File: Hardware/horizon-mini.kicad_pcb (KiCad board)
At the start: 2 copper layers, 35 x 35.5 mm, 81 parts, among them J2 Conn_01x02_Pin, J3 Micro_SD_Card_Det1, J7 USB_C_Receptacle_USB2.0_16P, J8 Conn_02x03_Counter_Clockwise, Q1 BSS138, Q10 DMG2301L, U1 TPS82130, U16 AP2112K-3.3, U2 TPS61092, U3 LTC4412xS6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

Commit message: Finally done... DRC look good, PCB is good, and schematic looks good!
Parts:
- added R5: 10kΩ, Resistor_SMD:R_0402_1005Metric, B.Cu at (151.1, 118.9)
- C78: footprint Capacitor_SMD:C_0603_1608Metric -> Capacitor_SMD:C_0402_1005Metric
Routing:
- net MISO TMCU: track 50.7 -> 47.8 mm, vias 7 -> 4
- net +3.3V: track 155.7 -> 158.2 mm, vias 9 -> 10
- net GND: track 120.0 -> 121.6 mm, vias 31 -> 134
- net CS_NAND MMCU: track 32.2 -> 33.6 mm
- net CS_SD MMCU: track 34.0 -> 35.2 mm
- net MOSI TMCU: track 32.4 -> 33.2 mm, vias 4 -> 3
- net BUZZER: track 41.3 -> 42.0 mm
- net Net-(U7-~{CS}): track 2.13 -> 1.47 mm
- net +5V: track 9.82 -> 9.23 mm
- net (no net): vias 0 -> 2
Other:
- board size 35 x 35.5 mm -> 36 x 36 mm

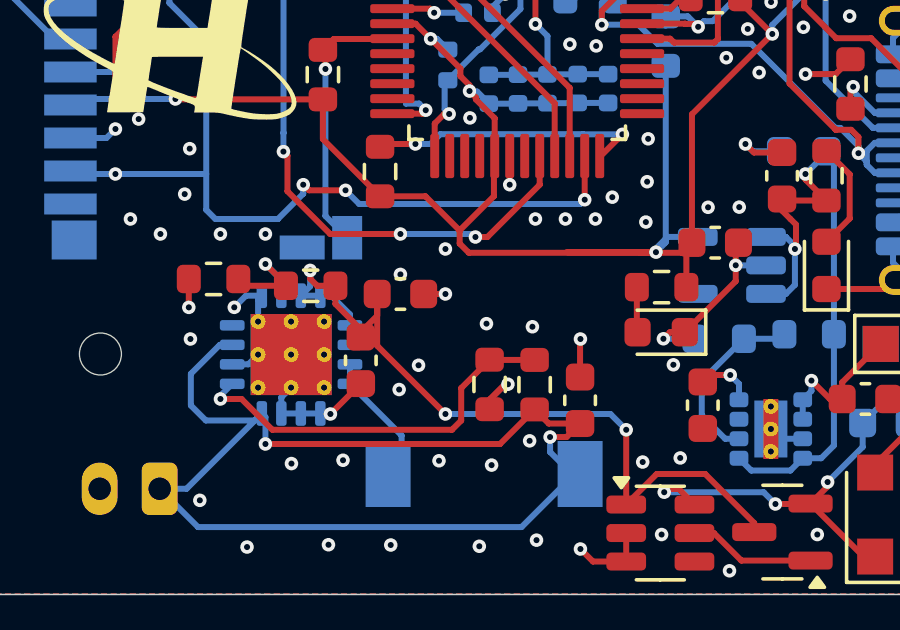
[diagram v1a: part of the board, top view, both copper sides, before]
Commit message: now final ;)... Needed to switch the 100uF to 0206, since 0603's for that just don't exist!
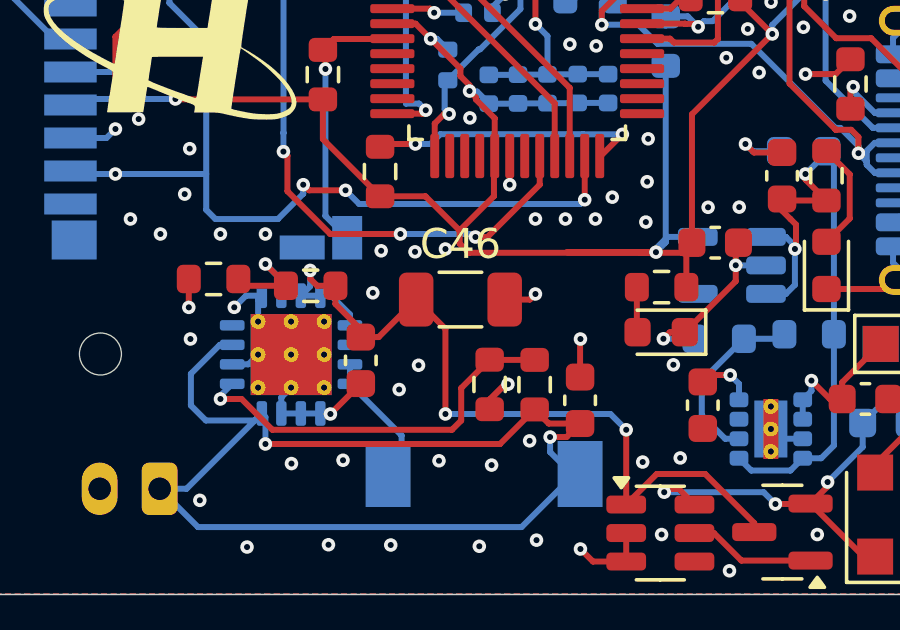
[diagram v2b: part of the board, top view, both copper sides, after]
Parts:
- C46: value 100u -> 100uF; footprint Capacitor_SMD:C_0603_1608Metric -> Capacitor_SMD:C_1206_3216Metric
- moved C46 2.01 mm to (151.5, 126.7)
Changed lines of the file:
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@@
 		)
 	)
-	(footprint "Capacitor_SMD:C_0603_1608Metric"
+	(footprint "Capacitor_SMD:C_1206_3216Metric"
 		(layer "F.Cu")
-		(at 149.5 126.5)
-		(descr "Capacitor SMD 0603 (1608 Metric), square (rectangular) end terminal, IPC-7351 nominal, (Body size source: IPC-SM-782 page 76, https://www.pcb-3d.com/wordpress/wp-content/uploads/ipc-sm-782a_amendment_1_and_2.pdf), generated with kicad-footprint-generator")
+		(at 151.5 126.685172)
+		(descr "Capacitor SMD 1206 (3216 Metric), square (rectangular) end terminal, IPC-7351 nominal, (Body size source: IPC-SM-782 page 76, https://www.pcb-3d.com/wordpress/wp-content/uploads/ipc-sm-782a_amendment_1_and_2.pdf), generated with kicad-footprint-generator")
 		(tags "capacitor")
 		(property "Reference" "C46"
-			(at 0 -1.43 0)
+			(at 0 -1.85 0)
 			(layer "F.SilkS")
-			(hide yes)
 			(effects
 				(font
@@
 			)
 		)
-		(property "Value" "100u"
-			(at 0 1.43 0)
+		(property "Value" "100uF"
+			(at 0 1.85 0)
 			(layer "F.Fab")
 			(effects
@@
 			)
 		)
-		(property "Description" "Polarized capacitor, US symbol"
+		(property "Description" ""
 			(at 0 0 0)
 			(layer "F.Fab")
@@
 		(attr smd)
 		(fp_line
-			(start -0.14058 -0.51)
-			(end 0.14058 -0.51)
+			(start -0.711252 -0.91)
+			(end 0.711252 -0.91)
 			(stroke
 				(width 0.12)
@@
 		)
 		(fp_line
-			(start -0.14058 0.51)
-			(end 0.14058 0.51)
+			(start -0.711252 0.91)
+			(end 0.711252 0.91)
 			(stroke
 				(width 0.12)
@@
 		)
 		(fp_line
-			(start -1.48 -0.73)
-			(end 1.48 -0.73)
+			(start -2.3 -1.15)
+			(end 2.3 -1.15)
 			(stroke
 				(width 0.05)
@@
 		)
 		(fp_line
-			(start -1.48 0.73)
-			(end -1.48 -0.73)
+			(start -2.3 1.15)
+			(end -2.3 -1.15)
 			(stroke
 				(width 0.05)
@@
 		)
 		(fp_line
-			(start 1.48 -0.73)
-			(end 1.48 0.73)
+			(start 2.3 -1.15)
+			(end 2.3 1.15)
 			(stroke
 				(width 0.05)
@@
 		)
 		(fp_line
-			(start 1.48 0.73)
-			(end -1.48 0.73)
+			(start 2.3 1.15)
+			(end -2.3 1.15)
 			(stroke
 				(width 0.05)
@@
 		)
 		(fp_line
-			(start -0.8 -0.4)
-			(end 0.8 -0.4)
+			(start -1.6 -0.8)
+			(end 1.6 -0.8)
 			(stroke
 				(width 0.1)
@@
 		)
 		(fp_line
-			(start -0.8 0.4)
-			(end -0.8 -0.4)
+			(start -1.6 0.8)
+			(end -1.6 -0.8)
 			(stroke
 				(width 0.1)
@@
 		)
 		(fp_line
-			(start 0.8 -0.4)
-			(end 0.8 0.4)
+			(start 1.6 -0.8)
+			(end 1.6 0.8)
 			(stroke
 				(width 0.1)
@@
 		)
 		(fp_line
-			(start 0.8 0.4)
-			(end -0.8 0.4)
+			(start 1.6 0.8)
+			(end -1.6 0.8)
 			(stroke
 				(width 0.1)
@@
 			(effects
 				(font
-					(size 0.4 0.4)
-					(thickness 0.06)
+					(size 0.8 0.8)
+					(thickness 0.12)
 				)
 			)
 		)
 		(pad "1" smd roundrect
-			(at -0.775 0)
-			(size 0.9 0.95)
+			(at -1.475 0)
+			(size 1.15 1.8)
 			(layers "F.Cu" "F.Mask" "F.Paste")
-			(roundrect_rratio 0.25)
+			(roundrect_rratio 0.217391)
 			(net 9 "bat")
 			(pintype "passive")
 		)
 		(pad "2" smd roundrect
-			(at 0.775 0)
-			(size 0.9 0.95)
+			(at 1.475 0)
+			(size 1.15 1.8)
 			(layers "F.Cu" "F.Mask" "F.Paste")
-			(roundrect_rratio 0.25)
+			(roundrect_rratio 0.217391)
 			(net 3 "GND")
 			(pintype "passive")
 		)
 		(embedded_fonts no)
-		(model "${KICAD9_3DMODEL_DIR}/Capacitor_SMD.3dshapes/C_0603_1608Metric.step"
+		(model "${KICAD9_3DMODEL_DIR}/Capacitor_SMD.3dshapes/C_1206_3216Metric.step"
 			(offset
 				(xyz 0 0 0)
@@
 	)
 	(segment
+		(start 153.814828 126.685172)
+		(end 154 126.5)
+		(width 0.2)
+		(layer "F.Cu")
+		(net 3)
+	)
+	(segment
 		(start 156.78381 115.488509)
 		(end 155.772319 116.5)
@@
 	)
 	(segment
+		(start 152.975 126.685172)
+		(end 153.814828 126.685172)
+		(width 0.2)
+		(layer "F.Cu")
+		(net 3)
+	)
+	(segment
 		(start 145.5 106.5)
 		(end 145.5 106.500486)
@@
 	)
 	(segment
-		(start 150.275 126.5)
-		(end 151 126.5)
-		(width 0.2)
-		(layer "F.Cu")
-		(net 3)
-	)
-	(segment
 		(start 164.005823 119.169177)
 		(end 163.00209 119.169177)
@@
 	)
 	(via
-		(at 149.49958 125.84684)
+		(at 154 126.5)
 		(size 0.45)
 		(drill 0.2)
 		(layers "F.Cu" "B.Cu")
-		(free yes)
 		(net 3)
 	)
@@
 	)
 	(via
-		(at 153.89965 127.591575)
+		(at 155 106)
 		(size 0.45)
 		(drill 0.2)
@@
 	)
 	(via
-		(at 155 106)
+		(at 149.986212 125.094017)
 		(size 0.45)
 		(drill 0.2)
@@
 	)
 	(via
+		(at 148.579415 126.461106)
+		(size 0.45)
+		(drill 0.2)
+		(layers "F.Cu" "B.Cu")
+		(free yes)
+		(net 3)
+	)
+	(via
 		(at 149.457035 129.684332)
 		(size 0.45)
@@
 	)
 	(via
+		(at 148.857371 125.059981)
+		(size 0.45)
+		(drill 0.2)
+		(layers "F.Cu" "B.Cu")
+		(free yes)
+		(net 3)
+	)
+	(via
 		(at 167.5 131)
 		(size 0.45)
@@
 	)
 	(via
-		(at 151 126.5)
-		(size 0.45)
-		(drill 0.2)
-		(layers "F.Cu" "B.Cu")
-		(net 3)
-	)
-	(via
 		(at 153.778211 114.87454)
 		(size 0.45)
@@
 	)
 	(via
-		(at 152.368057 127.489468)
-		(size 0.45)
-		(drill 0.2)
-		(layers "F.Cu" "B.Cu")
-		(free yes)
-		(net 3)
-	)
-	(via
 		(at 145 124.5)
 		(size 0.45)
@@
 	)
 	(segment
-		(start 148.725 127.225)
-		(end 148.725 126.5)
-		(width 0.2)
-		(layer "F.Cu")
-		(net 9)
-	)
-	(segment
 		(start 147.333521 126.833521)
 		(end 147.333521 126.225832)
@@
 	)
 	(segment
-		(start 148.1793 127.7707)
-		(end 148.725 127.225)
+		(start 159.65887 132.5)
+		(end 158.043536 132.5)
 		(width 0.2)
 		(layer "F.Cu")
@@
 	)
 	(segment
-		(start 159.65887 132.5)
-		(end 158.043536 132.5)
+		(start 148.1793 127.936829)
+		(end 148.1793 127.6793)
 		(width 0.2)
 		(layer "F.Cu")
@@
 	)
 	(segment
-		(start 148.1793 127.936829)
-		(end 148.1793 127.6793)
+		(start 151 127.660172)
+		(end 151 130.5)
 		(width 0.2)
 		(layer "F.Cu")
@@
 	)
 	(segment
-		(start 148.1793 127.936829)
-		(end 148.1793 127.7707)
+		(start 150.025 126.685172)
+		(end 151 127.660172)
 		(width 0.2)
 		(layer "F.Cu")
@@
 	)
 	(segment
-		(start 148.725 128.225)
-		(end 151 130.5)
+		(start 148.1793 127.936829)
+		(end 148.1793 127.7707)
 		(width 0.2)
 		(layer "F.Cu")
@@
 	)
 	(segment
-		(start 148.725 126.5)
-		(end 148.725 128.225)
+		(start 148.436829 127.936829)
+		(end 148.1793 127.936829)
 		(width 0.2)
 		(layer "F.Cu")
@@
 		(width 0.2)
 		(layer "F.Cu")
+		(net 9)
+	)
+	(segment
+		(start 148.1793 127.936829)
+		(end 148.773343 127.936829)
+		(width 0.2)
+		(layer "F.Cu")
+		(net 9)
+	)
+	(segment
+		(start 148.773343 127.936829)
+		(end 150.025 126.685172)
+		(width 0.2)
+		(layer "F.Cu")

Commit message: final take 2 ;). Now no JLC DFM errors either!
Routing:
- net SWCLK DMCU-2: track 23.4 -> 24.3 mm
- net nRESET DMCU-2: track 15.9 -> 16.7 mm
- net Net-(J2-Pin_1): track 40.0 -> 40.7 mm
- net Net-(U6-~{WP}/IO_{2}): track 2.26 -> 2.94 mm
- net GND: track 122.0 -> 122.6 mm, vias 134 -> 133
- net (no net): vias 2 -> 1
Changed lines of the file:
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@@
 		(net 0)
 	)
-	(via
-		(at 153.806053 131.395031)
-		(size 0.45)
-		(drill 0.2)
-		(layers "F.Cu" "B.Cu")
-		(net 0)
-	)
 	(segment
 		(start 160.825 116.420873)
@@
 	)
 	(segment
+		(start 158.140133 128.356649)
+		(end 158.394694 128.356649)
+		(width 0.2)
+		(layer "F.Cu")
+		(net 3)
+	)
+	(segment
 		(start 163.5 102.68625)
 		(end 163.7375 102.68625)
@@
 	)
 	(segment
-		(start 166.192177 126.33376)
-		(end 166.494688 126.031249)
+		(start 158.394694 128.356649)
+		(end 158.978011 127.773332)
 		(width 0.2)
 		(layer "F.Cu")
@@
 	)
 	(segment
-		(start 158.484795 127.773332)
-		(end 158.265511 127.992616)
+		(start 166.192177 126.33376)
+		(end 166.494688 126.031249)
 		(width 0.2)
 		(layer "F.Cu")
@@
 	)
 	(segment
-		(start 158.978011 127.773332)
-		(end 158.484795 127.773332)
-		(width 0.2)
-		(layer "F.Cu")
-		(net 3)
-	)
-	(segment
 		(start 167.975309 122.55)
 		(end 167.969011 122.556298)
@@
 	)
 	(via
-		(at 163.96108 111.336729)
-		(size 0.45)
-		(drill 0.2)
-		(layers "F.Cu" "B.Cu")
-		(free yes)
-		(net 3)
-	)
-	(via
 		(at 168.961765 109.593177)
 		(size 0.45)
@@
 	)
 	(via
-		(at 158.265511 127.992616)
+		(at 158.140133 128.356649)
 		(size 0.45)
 		(drill 0.2)
@@
 	)
 	(segment
-		(start 158.265511 127.992616)
-		(end 159.298449 127.992616)
+		(start 155.410436 119.171724)
+		(end 155.409353 119.170641)
 		(width 0.2)
 		(layer "B.Cu")
@@
 	)
 	(segment
-		(start 155.410436 119.171724)
-		(end 155.409353 119.170641)
+		(start 159.298449 127.992616)
+		(end 158.504166 127.992616)
 		(width 0.2)
 		(layer "B.Cu")
@@
 	)
 	(segment
+		(start 158.504166 127.992616)
+		(end 158.140133 128.356649)
+		(width 0.2)
+		(layer "B.Cu")
+		(net 3)
+	)
+	(segment
 		(start 161.6025 103.97375)
 		(end 161.6025 104.692496)
@@
 	)
 	(segment
-		(start 155.038475 131.267931)
-		(end 155.488475 130.817931)
-		(width 0.2)
-		(layer "F.Cu")
-		(net 6)
-	)
-	(segment
 		(start 153.973014 130.347316)
 		(end 152.82033 131.5)
@@
 	)
 	(segment
-		(start 154.488475 131.267931)
-		(end 155.038475 131.267931)
+		(start 154 131.75)
+		(end 154.482069 131.267931)
 		(width 0.2)
 		(layer "F.Cu")
@@
 	)
 	(segment
+		(start 155.038475 131.267931)
+		(end 155.488475 130.817931)
+		(width 0.2)
+		(layer "F.Cu")
+		(net 6)
+	)
+	(segment
 		(start 154.443629 130.817931)
 		(end 153.973014 130.347316)
@@
 		(net 6)
 	)
+	(segment
+		(start 154.482069 131.267931)
+		(end 155.038475 131.267931)
+		(width 0.2)
+		(layer "F.Cu")
+		(net 6)
+	)
 	(via
-		(at 154.488475 131.267931)
+		(at 154 131.75)
 		(size 0.45)
 		(drill 0.2)
@@
 	)
 	(segment
-		(start 155.488475 132.767931)
-		(end 154.488475 131.767931)
+		(start 154.488475 131.767931)
+		(end 155.488475 132.767931)
 		(width 0.2)
 		(layer "B.Cu")
@@
 	)
 	(segment
-		(start 154.488475 131.767931)
-		(end 154.488475 131.267931)
+		(start 154 131.75)
+		(end 154.017931 131.767931)
 		(width 0.2)
 		(layer "B.Cu")
@@
 	)
 	(segment
+		(start 154.017931 131.767931)
+		(end 154.488475 131.767931)
+		(width 0.2)
+		(layer "B.Cu")
+		(net 6)
+	)
+	(segment
 		(start 142.514485 130.215549)
 		(end 142.514485 129.160426)
@@
 	)
 	(segment
-		(start 151.642634 113.576009)
-		(end 151.642634 112.804685)
-		(width 0.2)
-		(layer "F.Cu")
-		(net 30)
-	)
-	(segment
-		(start 153.639287 110.808032)
-		(end 165.691968 110.808032)
+		(start 153.947319 110.5)
+		(end 166 110.5)
 		(width 0.2)
 		(layer "F.Cu")
@@
 	(segment
 		(start 151.642634 112.804685)
-		(end 153.639287 110.808032)
+		(end 153.947319 110.5)
 		(width 0.2)
 		(layer "F.Cu")
@@
 	)
 	(segment
-		(start 165.691968 110.808032)
-		(end 166 110.5)
+		(start 151.642634 113.576009)
+		(end 151.642634 112.804685)
 		(width 0.2)
 		(layer "F.Cu")
@@
 	)
 	(segment
-		(start 166.25 113)
+		(start 167.175 113.285)
 		(end 167.46 113)
 		(width 0.2)
@@
 	)
 	(segment
-		(start 163.399 112.526)
-		(end 163.551 112.374)
+		(start 164.3375 111.5875)
+		(end 164.5875 111.5875)
 		(width 0.2)
 		(layer "F.Cu")
@@
 	)
 	(segment
-		(start 161.341034 111.877458)
-		(end 161.989576 112.526)
+		(start 161.989576 112.526)
+		(end 161.341034 111.877458)
 		(width 0.2)
 		(layer "F.Cu")
@@
 	)
 	(segment
-		(start 167.175 113.285)
-		(end 167.46 113)
+		(start 163.6625 111.5875)
+		(end 162.724 112.526)
 		(width 0.2)
 		(layer "F.Cu")
@@
 	)
 	(segment
-		(start 163.675 112.25)
-		(end 165.5 112.25)
+		(start 161.341034 111.877458)
+		(end 155.569861 111.877458)
 		(width 0.2)
 		(layer "F.Cu")
@@
 	)
 	(segment
-		(start 161.989576 112.526)
-		(end 163.399 112.526)
+		(start 154.642634 112.804685)
+		(end 154.642634 113.576009)
 		(width 0.2)
 		(layer "F.Cu")
@@
 	)
 	(segment
-		(start 154.642634 113.576009)
-		(end 154.642634 112.804685)
+		(start 162.724 112.526)
+		(end 161.989576 112.526)
 		(width 0.2)
 		(layer "F.Cu")
@@
 	)
 	(segment
-		(start 154.642634 112.804685)
-		(end 155.569861 111.877458)
+		(start 164.5875 111.5875)
+		(end 166 113)
 		(width 0.2)
 		(layer "F.Cu")
@@
 	)
 	(segment
-		(start 163.551 112.374)
-		(end 163.675 112.25)
+		(start 155.569861 111.877458)
+		(end 154.642634 112.804685)
 		(width 0.2)
 		(layer "F.Cu")
@@
 	)
 	(segment
-		(start 155.569861 111.877458)
-		(end 161.341034 111.877458)
+		(start 166 113)
+		(end 167.46 113)
 		(width 0.2)
 		(layer "F.Cu")
@@
 	)
 	(segment
-		(start 165.5 112.25)
-		(end 166.25 113)
+		(start 164.3375 111.5875)
+		(end 163.6625 111.5875)
 		(width 0.2)
 		(layer "F.Cu")
@@
 	)
 	(via
-		(at 163.551 112.374)
+		(at 164.3375 111.5875)
 		(size 0.45)
 		(drill 0.2)
@@
 	)
 	(segment
-		(start 163.551 112.5)
-		(end 163.564491 112.513491)
-		(width 0.2)
-		(layer "B.Cu")
-		(net 31)
-	)
-	(segment
-		(start 163.564491 112.513491)
-		(end 164.20484 112.513491)
+		(start 163.88984 112.03516)
+		(end 164.3375 111.5875)
 		(width 0.2)
 		(layer "B.Cu")
@@
 	)
 	(segment
-		(start 163.551 112.374)
-		(end 163.551 112.5)
+		(start 163.88984 112.513491)
+		(end 163.88984 112.03516)
 		(width 0.2)
 		(layer "B.Cu")
@@
 	)
 	(segment
-		(start 162.651 111.849)
-		(end 168.849 111.849)
+		(start 162.5 112)
+		(end 162.5 111.5)
 		(width 0.2)
 		(layer "F.Cu")
@@
 	)
 	(segment
-		(start 162.5 112)
-		(end 162.651 111.849)
+		(start 162.5 111.5)
+		(end 162.890968 111.109032)
 		(width 0.2)
 		(layer "F.Cu")
@@
 	)
 	(segment
+		(start 165.849 111.849)
+		(end 168.849 111.849)
+		(width 0.2)
+		(layer "F.Cu")
+		(net 32)
+	)
+	(segment
+		(start 165.109032 111.109032)
+		(end 165.849 111.849)
+		(width 0.2)
+		(layer "F.Cu")
+		(net 32)
+	)
+	(segment
+		(start 162.890968 111.109032)
+		(end 165.109032 111.109032)
+		(width 0.2)
+		(layer "F.Cu")
+		(net 32)
+	)
+	(segment
 		(start 168.849 111.849)
 		(end 170 113)
@@
 	)
 	(segment
-		(start 149.3385 101.3385)
-		(end 149.382419 101.382419)
+		(start 149.382419 101.53903)
+		(end 148.53903 101.53903)
 		(width 0.2)
 		(layer "F.Cu")
@@
 	)
 	(segment
-		(start 148.649112 101.472623)
-		(end 148.783235 101.3385)
-		(width 0.2)
-		(layer "F.Cu")
-		(net 40)
-	)
-	(segment
-		(start 149.382419 101.382419)
-		(end 149.382419 101.53903)
-		(width 0.2)
-		(layer "F.Cu")
-		(net 40)
-	)
-	(segment
-		(start 148.783235 101.3385)
-		(end 149.3385 101.3385)
+		(start 148.53903 101.53903)
+		(end 148.25 101.25)
 		(width 0.2)
 		(layer "F.Cu")
@@
 	)
 	(via
-		(at 148.649112 101.472623)
+		(at 148.25 101.25)
 		(size 0.45)
 		(drill 0.2)
@@
 	)
 	(segment
-		(start 149.246745 102.085245)
-		(end 149.246745 102.526284)
-		(width 0.2)
-		(layer "B.Cu")
-		(net 40)
-	)
-	(segment
-		(start 148.649112 101.472623)
-		(end 148.649112 101.487612)
+		(start 149.246745 102.526284)
+		(end 149.246745 102.246745)
 		(width 0.2)
 		(layer "B.Cu")
@@
 	)
 	(segment
-		(start 148.649112 101.487612)
-		(end 149.246745 102.085245)
+		(start 149.246745 102.246745)
+		(end 148.25 101.25)
 		(width 0.2)
 		(layer "B.Cu")

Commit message: the final final one
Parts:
- C46: value 100uF -> 100u
- J2: footprint Connector_JST:JST_PH_B2B-PH-K_1x02_P2.00mm_Vertical -> TerminalBlock_MetzConnect:TerminalBlock_MetzConnect_Type059_RT06302HBWC_1x02_P3.50mm_Horizontal; moved to F.Cu
- moved J2 3.25 mm to (138.3, 132.2), turned to 0 degrees
- moved REF** 1.35 mm to (139.0, 127.2)
- moved C40 0.45 mm to (165.7, 131.2)
- moved D5 0.41 mm to (170.5, 129.7)
- moved U1 0.40 mm to (161.8, 131.4)
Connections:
- D13 pad 1: VBUS -> +5V
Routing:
- net Net-(J2-Pin_1): track 40.7 -> 55.1 mm, vias 2 -> 1
- net GND: track 122.6 -> 135.2 mm
- net +5V: track 9.23 -> 13.4 mm, vias 1 -> 3
- net POWAAAA: track 18.6 -> 19.5 mm
- net Net-(D13-A): track 29.1 -> 28.3 mm

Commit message: i̶t̶'s̶ a̶l̶l̶ d̶o̶w̶n̶ h̶i̶l̶l̶ f̶r̶o̶m̶ h̶e̶r̶e̶ f̶r̶i̶e̶n̶d̶s̶
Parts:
- removed BZ2: Buzzer, Buzzer_Beeper:MagneticBuzzer_PUI_AT-0927-TT-6-R
- removed Q1: BSS138, Package_TO_SOT_SMD:SOT-23
- removed R1: 2k2, Resistor_SMD:R_0603_1608Metric
- C1, C11, C12, C3, C4, C6, C7, C78, C8, C9, D1, J3, R13, R18, R19, R20, R21, R27, R29, R5: moved to F.Cu
- D14, G***, R11, R15, R23: moved to B.Cu
- R6: footprint Resistor_SMD:R_0603_1608Metric -> Resistor_SMD:R_0805_2012Metric
- moved REF** 41.2 mm to (179.8, 114.0)
- moved REF** 39.8 mm to (178.8, 129.7)
- moved R6 35.4 mm to (198.3, 131.8)
- moved C14 35.4 mm to (194.8, 134.0)
- moved C17 35.4 mm to (190.7, 133.8)
- moved C46 35.4 mm to (186.7, 130.5)
- moved D11 35.4 mm to (193.4, 131.5)
- moved L7 35.4 mm to (187.5, 136.3)
- moved Q10 35.4 mm to (197.4, 138.2)
- moved R14 35.4 mm to (193.4, 130.0)
- moved R3 35.4 mm to (189.1, 133.3)
- moved R4 35.4 mm to (187.6, 133.3)
- moved U1 35.4 mm to (197.0, 135.2)
- moved U3 35.4 mm to (193.3, 138.2)
- moved R7 35.1 mm to (195.1, 131.7)
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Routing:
- net GND: track 135.2 -> 35.1 mm, vias 133 -> 12
- net +3.3V: track 158.2 -> 83.2 mm, vias 10 -> 4
- net Net-(J2-Pin_1): track 55.1 -> 0.00 mm, vias 1 -> 0
- net BUZZER: track 42.0 -> 0.00 mm, vias 4 -> 0
- net MISO TMCU: track 47.8 -> 16.1 mm, vias 4 -> 1
- net I2C0_SDA: track 36.2 -> 5.60 mm, vias 2 -> 0
- net CS_SD MMCU: track 35.2 -> 5.18 mm, vias 5 -> 2
- net bat: track 28.1 -> 0.00 mm, vias 3 -> 0
- net SCK TMCU: track 38.7 -> 12.9 mm, vias 2 -> 1
- net Net-(U16-EN): track 22.6 -> 0.00 mm, vias 2 -> 0
- net MOSI TMCU: track 33.1 -> 11.8 mm, vias 3 -> 1
- net CS_NAND MMCU: track 33.6 -> 13.3 mm, vias 3 -> 1
- net I2C0_SCL: track 33.8 -> 14.1 mm, vias 3 -> 0
- net POWAAAA: track 19.5 -> 0.00 mm, vias 3 -> 0
- net D+ DMCU-2: track 24.0 -> 4.51 mm, vias 2 -> 0
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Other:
- board size 36 x 36 mm -> 34 x 34 mm

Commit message: getting somewhere take 2
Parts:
- C37, C40, D13, D5, L7, R6, R7, U1, U16, U2: moved to F.Cu
- moved R10 45.5 mm to (157.1, 122.5), turned to 0 degrees
- moved D11 43.4 mm to (156.4, 108.7), turned to 0 degrees
- moved R14 41.9 mm to (156.4, 110.2), turned to 0 degrees
- moved U2 41.3 mm to (155.3, 126.0), turned to 0 degrees
- moved Q10 39.9 mm to (163.2, 117.5), turned to 0 degrees
- moved U3 39.7 mm to (159.6, 117.3), turned to 90 degrees
- moved R9 39.6 mm to (154.1, 122.5), turned to 0 degrees
- moved C39 38.7 mm to (154.1, 121.0), turned to 0 degrees
- moved D13 38.4 mm to (158.0, 104.8), turned to 90 degrees
- moved D5 35.1 mm to (160.9, 122.9), turned to 0 degrees
- moved U16 35.0 mm to (159.6, 113.1), turned to -90 degrees
- moved U1 31.7 mm to (167.1, 124.5), turned to 0 degrees
- moved R6 30.7 mm to (168.0, 127.2), turned to 0 degrees
- moved L7 30.2 mm to (157.5, 132.6)
- moved R7 29.9 mm to (167.4, 120.4)
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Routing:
- net Net-(U16-EN): track 0.00 -> 33.4 mm, vias 0 -> 2
- net bat: track 0.00 -> 20.1 mm
- net Net-(J2-Pin_1): track 0.00 -> 14.4 mm
- net POWAAAA: track 0.00 -> 13.8 mm
- net Net-(U1-FB): track 0.00 -> 7.89 mm
- net Net-(L7-Pad2): track 0.00 -> 6.68 mm
- net +5V: track 0.00 -> 6.66 mm
- net +3.3V: track 83.2 -> 89.8 mm
- net Net-(D13-A): track 15.4 -> 21.7 mm
- net Net-(U2-LBI): track 0.00 -> 5.50 mm
- net Net-(D6-K): track 0.00 -> 4.65 mm
- net GND: track 35.1 -> 39.0 mm, vias 12 -> 14
- net Net-(Q10-G): track 0.00 -> 3.65 mm
- net Net-(U2-FB): track 0.00 -> 2.70 mm
- net Net-(D9-A): track 0.00 -> 1.66 mm
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
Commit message: DRC and some PCB routing stuff
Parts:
- moved G*** 11.0 mm to (153.0, 119.0)
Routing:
- net GND: track 39.0 -> 77.7 mm, vias 14 -> 25
- net SD_DETECT: track 4.66 -> 28.7 mm
- net +3.3V: track 89.8 -> 111.7 mm, vias 4 -> 6
- net +5V: track 6.66 -> 24.9 mm, vias 0 -> 2
- net D+ DMCU-2: track 4.51 -> 11.5 mm
- net POWAAAA: track 13.8 -> 20.1 mm
- net Net-(J2-Pin_1): track 14.4 -> 20.2 mm, vias 0 -> 2
- net CS_IMU TMCU: track 0.00 -> 1.22 mm
